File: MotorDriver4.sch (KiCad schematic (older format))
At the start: 38 parts, among them J24 43045-0802, J25 53426-0410, U49 MAX40056FAUA+, U50 DRV8312DDWR, U51 MAX40056FAUA+, U52 MIC2090-2YM5-TR

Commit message: PVT
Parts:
- C200: renamed from C208; footprint Capacitor-Chip:C_CHIP_1608_Reflow -> Capacitor-Chip:C_CHIP_1005_Hand_NoSilk; PartName GRM188R61E105KA12D -> TMK105BJ105MV-F
- C201: renamed from C209; PartName C1005X5R1V105K050BE -> TMK105BJ105MV-F
- C202: renamed from C210; PartName C1005X5R1V105K050BE -> TMK105BJ105MV-F
- C203: renamed from C211; footprint Capacitor-Chip:C_CHIP_1608_Reflow -> Capacitor-Chip:C_CHIP_1005_Hand_NoSilk; PartName GRM188R61E105KA12D -> TMK105BJ105MV-F
- C204: renamed from C212; footprint Capacitor-Chip:C_CHIP_1608_Reflow -> Capacitor-Chip:C_CHIP_1005_Hand_NoSilk; PartName GRM188R61E105KA12D -> TMK105BJ105MV-F
- C205: renamed from C213; footprint Capacitor-Chip:C_CHIP_1608_Reflow -> Capacitor-Chip:C_CHIP_1005_Hand_NoSilk; PartName GRM188R61E105KA12D -> TMK105BJ105MV-F
- C207: renamed from C215; PartName C1005X5R1V105K050BE -> TMK105BJ105MV-F
- C208: renamed from C216; PartName C1005X5R1V105K050BE -> TMK105BJ105MV-F
- C216: renamed from C224; PartName C1005X5R1V105K050BE -> TMK105BJ105MV-F
- R110: renamed from R125; value 2m -> 3m; PartName PMR18EZPJV2L0 -> PMR18EZPFV3L00
- R111: renamed from R126; value 2m -> 3m; PartName PMR18EZPJV2L0 -> PMR18EZPFV3L00
- renumbered C214 to C206, C217 to C209, C218 to C210, C219 to C211, C220 to C212, C221 to C213, C222 to C214, C223 to C215, L22 to L18, L23 to L19, L24 to L20, R121 to R106, R122 to R107, R123 to R108, R124 to R109, R127 to R112, R128 to R113, RA27 to RA28, RA28 to RA29, RA29 to RA30, U49 to U46, U50 to U47, U51 to U48, U52 to U49

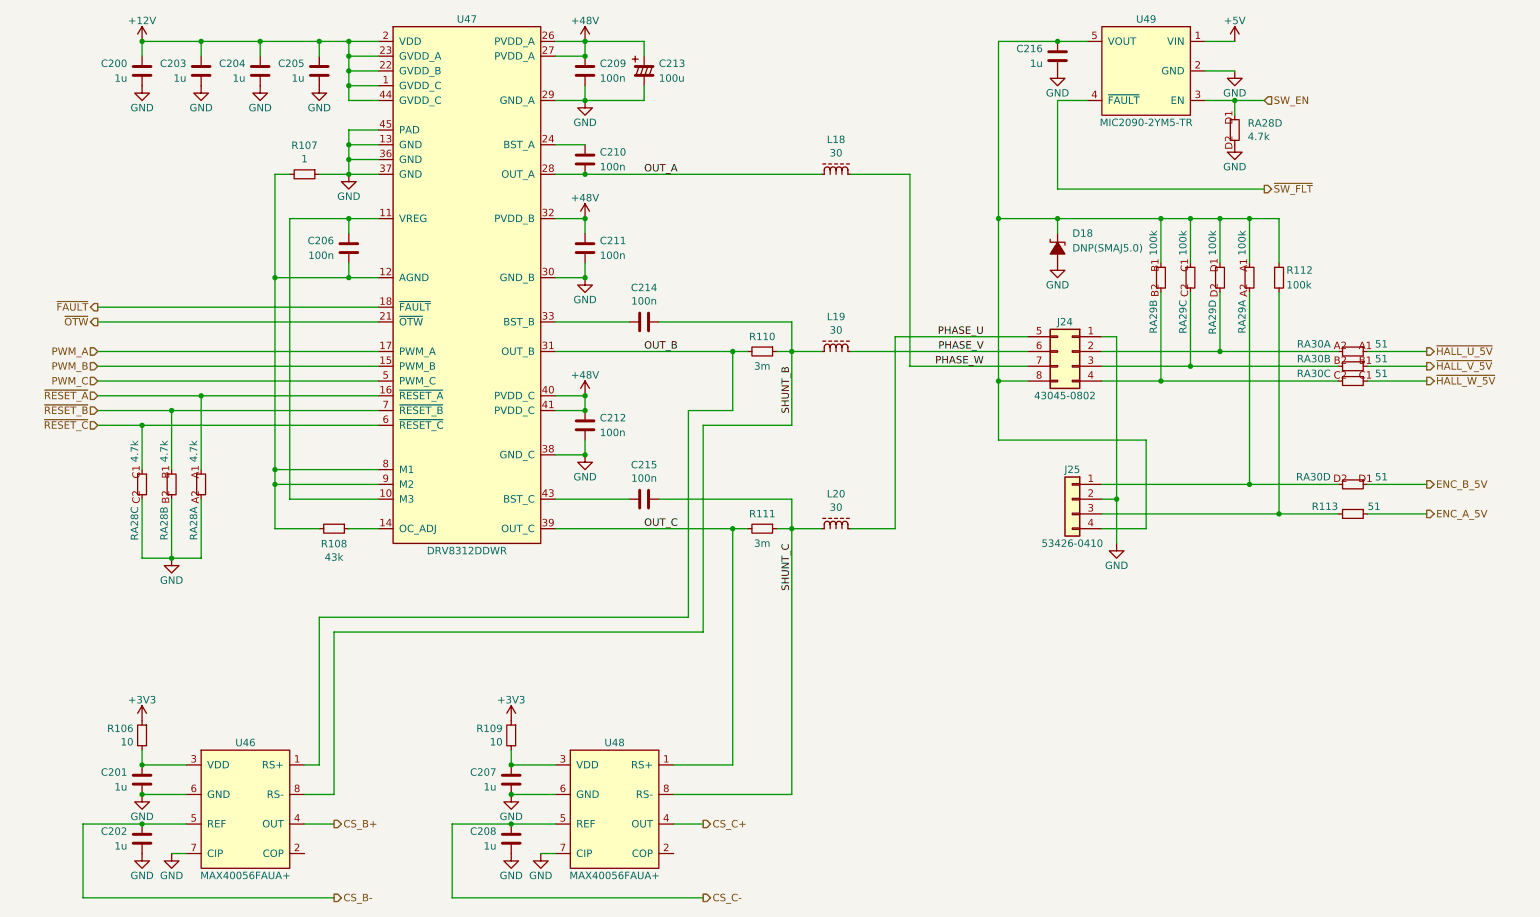
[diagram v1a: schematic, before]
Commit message: SBUにTVSダイオードを追加
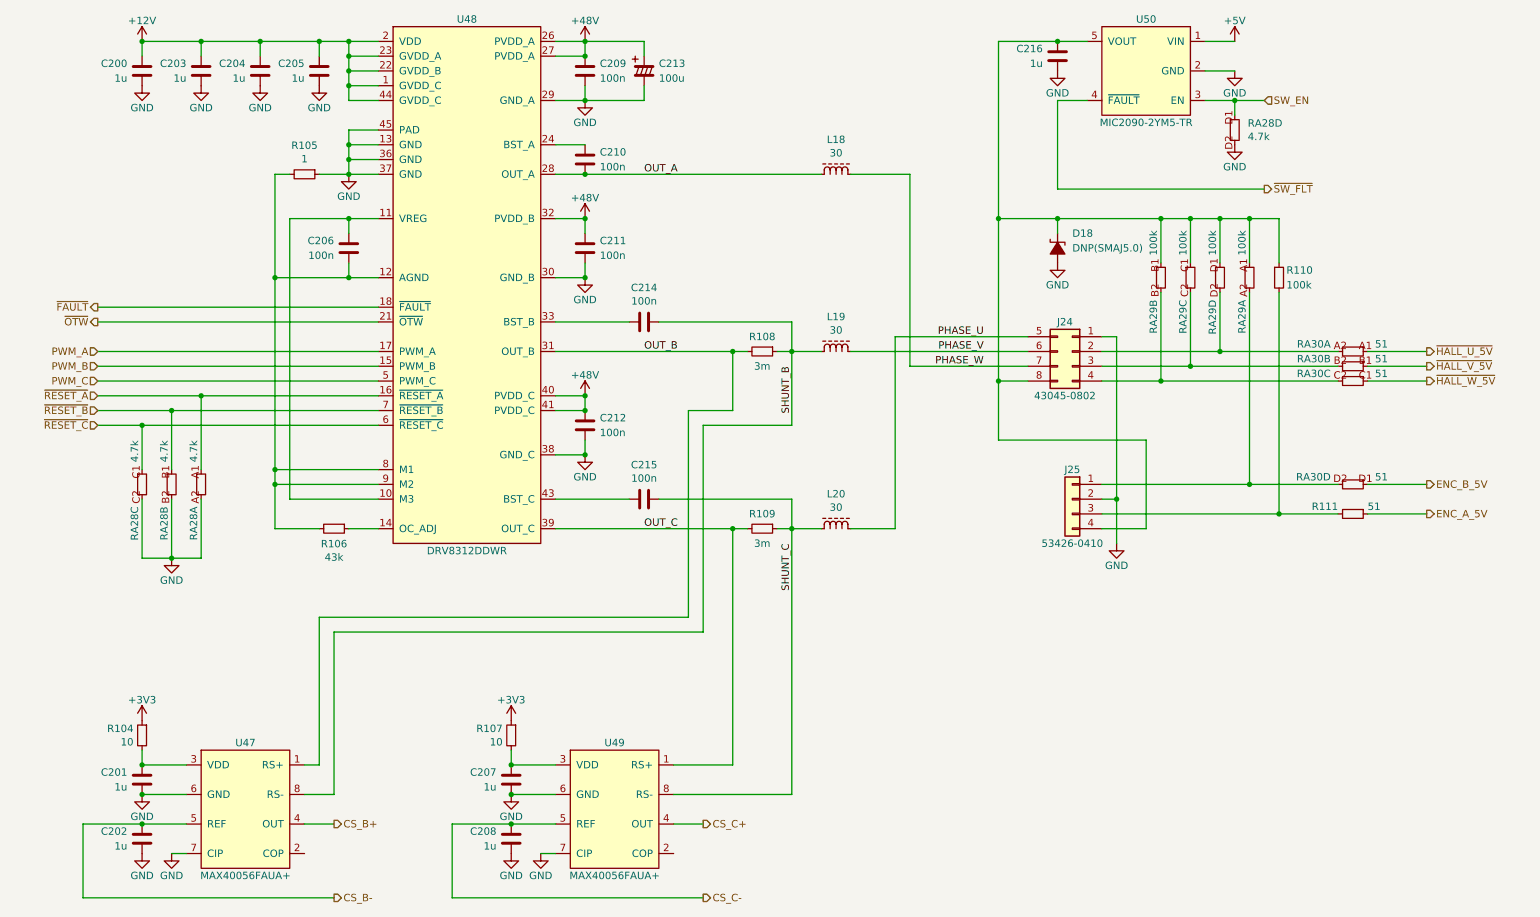
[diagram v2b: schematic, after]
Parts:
- renumbered R106 to R104, R107 to R105, R108 to R106, R109 to R107, R110 to R108, R111 to R109, R112 to R110, R113 to R111, U46 to U47, U47 to U48, U48 to U49, U49 to U50
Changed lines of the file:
@@
 AR Path="/5F237486/5E61F4E9" Ref="U?"  Part="1"
 AR Path="/5F259EEE/5E61F4E9" Ref="U?"  Part="1"
-AR Path="/5F259F7D/5E61F4E9" Ref="U47"  Part="1"
-F 0 "U47" H 4000 4750 50  0000 C CNN
+AR Path="/5F259F7D/5E61F4E9" Ref="U48"  Part="1"
+F 0 "U48" H 4000 4750 50  0000 C CNN
 F 1 "DRV8312DDWR" H 4000 1150 50  0000 C CNN
 F 2 "IC-SOP:HTSSOP44-W6.1_EP4.31x8.26" H 4000 2900 50  0001 C CNN
@@
 AR Path="/5F237486/5E61F5D9" Ref="R?"  Part="1"
 AR Path="/5F259EEE/5E61F5D9" Ref="R?"  Part="1"
-AR Path="/5F259F7D/5E61F5D9" Ref="R107"  Part="1"
-F 0 "R107" V 2705 2100 50  0000 C CNN
+AR Path="/5F259F7D/5E61F5D9" Ref="R105"  Part="1"
+F 0 "R105" V 2705 2100 50  0000 C CNN
 F 1 "1" V 2796 2100 50  0000 C CNN
 F 2 "Resistor-Chip:R_CHIP_1005_Hand_NoSilk" V 2950 2000 50  0001 C CNN
@@
 AR Path="/5F237486/5E61F5E3" Ref="R?"  Part="1"
 AR Path="/5F259EEE/5E61F5E3" Ref="R?"  Part="1"
-AR Path="/5F259F7D/5E61F5E3" Ref="R108"  Part="1"
-F 0 "R108" V 3203 4500 50  0000 C CNN
+AR Path="/5F259F7D/5E61F5E3" Ref="R106"  Part="1"
+F 0 "R106" V 3203 4500 50  0000 C CNN
 F 1 "43k" V 3294 4500 50  0000 C CNN
 F 2 "Resistor-Chip:R_CHIP_1005_Hand_NoSilk" V 3150 4400 50  0001 C CNN
@@
 AR Path="/5F237486/5E61F5F8" Ref="R?"  Part="1"
 AR Path="/5F259EEE/5E61F5F8" Ref="R?"  Part="1"
-AR Path="/5F259F7D/5E61F5F8" Ref="R111"  Part="1"
-F 0 "R111" V 5900 4500 50  0000 C CNN
+AR Path="/5F259F7D/5E61F5F8" Ref="R109"  Part="1"
+F 0 "R109" V 5900 4500 50  0000 C CNN
 F 1 "3m" V 6100 4500 50  0000 C CNN
 F 2 "Resistor-Chip:R_CHIP_3216_Reflow" V 6050 4400 50  0001 C CNN
@@
 AR Path="/5F237486/5E61F605" Ref="R?"  Part="1"
 AR Path="/5F259EEE/5E61F605" Ref="R?"  Part="1"
-AR Path="/5F259F7D/5E61F605" Ref="R110"  Part="1"
-F 0 "R110" V 5900 3300 50  0000 C CNN
+AR Path="/5F259F7D/5E61F605" Ref="R108"  Part="1"
+F 0 "R108" V 5900 3300 50  0000 C CNN
 F 1 "3m" V 6100 3300 50  0000 C CNN
 F 2 "Resistor-Chip:R_CHIP_3216_Reflow" V 6050 3200 50  0001 C CNN
@@
 AR Path="/5F259EEE/5F1F5EA4" Ref="U?"  Part="1"
 AR Path="/5F259F40/5F1F5EA4" Ref="U?"  Part="1"
-AR Path="/5F259F7D/5F1F5EA4" Ref="U49"  Part="1"
-F 0 "U49" H 8600 1750 50  0000 C CNN
+AR Path="/5F259F7D/5F1F5EA4" Ref="U50"  Part="1"
+F 0 "U50" H 8600 1750 50  0000 C CNN
 F 1 "MIC2090-2YM5-TR" H 8600 1050 50  0000 C CNN
 F 2 "IC-SOT:SOT23-5" H 8600 1400 50  0001 C CNN
@@
 AR Path="/5F235A43/5F4ED90C" Ref="U?"  Part="1"
 AR Path="/5F237486/5F4ED90C" Ref="U?"  Part="1"
-AR Path="/5F259F7D/5F4ED90C" Ref="U46"  Part="1"
-F 0 "U46" H 2500 6850 50  0000 C CNN
+AR Path="/5F259F7D/5F4ED90C" Ref="U47"  Part="1"
+F 0 "U47" H 2500 6850 50  0000 C CNN
 F 1 "MAX40056FAUA+" H 2500 5950 50  0000 C CNN
 F 2 "IC-SOP:MSOP8" H 2500 6400 50  0001 C CNN
@@
 AR Path="/5F235A43/5F4ED912" Ref="U?"  Part="1"
 AR Path="/5F237486/5F4ED912" Ref="U?"  Part="1"
-AR Path="/5F259F7D/5F4ED912" Ref="U48"  Part="1"
-F 0 "U48" H 5000 6850 50  0000 C CNN
+AR Path="/5F259F7D/5F4ED912" Ref="U49"  Part="1"
+F 0 "U49" H 5000 6850 50  0000 C CNN
 F 1 "MAX40056FAUA+" H 5000 5950 50  0000 C CNN
 F 2 "IC-SOP:MSOP8" H 5000 6400 50  0001 C CNN
@@
 AR Path="/5F235A43/5F4ED978" Ref="R?"  Part="1"
 AR Path="/5F237486/5F4ED978" Ref="R?"  Part="1"
-AR Path="/5F259F7D/5F4ED978" Ref="R106"  Part="1"
-F 0 "R106" H 1858 5946 50  0000 L CNN
+AR Path="/5F259F7D/5F4ED978" Ref="R104"  Part="1"
+F 0 "R104" H 1858 5946 50  0000 L CNN
 F 1 "10" H 1858 5855 50  0000 L CNN
 F 2 "Resistor-Chip:R_CHIP_1005_Hand_NoSilk" V 1850 5800 50  0001 C CNN
@@
 AR Path="/5F235A43/5F4ED97E" Ref="R?"  Part="1"
 AR Path="/5F237486/5F4ED97E" Ref="R?"  Part="1"
-AR Path="/5F259F7D/5F4ED97E" Ref="R109"  Part="1"
-F 0 "R109" H 4358 5946 50  0000 L CNN
+AR Path="/5F259F7D/5F4ED97E" Ref="R107"  Part="1"
+F 0 "R107" H 4358 5946 50  0000 L CNN
 F 1 "10" H 4358 5855 50  0000 L CNN
 F 2 "Resistor-Chip:R_CHIP_1005_Hand_NoSilk" V 4350 5800 50  0001 C CNN
@@
 P 10000 4400
 AR Path="/5F235A43/5EA40EFB" Ref="R?"  Part="1"
-AR Path="/5F259F7D/5EA40EFB" Ref="R113"  Part="1"
-F 0 "R113" V 9950 4300 50  0000 R CNN
+AR Path="/5F259F7D/5EA40EFB" Ref="R111"  Part="1"
+F 0 "R111" V 9950 4300 50  0000 R CNN
 F 1 "51" V 9950 4500 50  0000 L CNN
 F 2 "Resistor-Chip:R_CHIP_1005_Hand_NoSilk" V 10050 4300 50  0001 C CNN
@@
 P 9500 2800
 AR Path="/5F235A43/5EA9B0A9" Ref="R?"  Part="1"
-AR Path="/5F259F7D/5EA9B0A9" Ref="R112"  Part="1"
-F 0 "R112" H 9550 2850 50  0000 L CNN
+AR Path="/5F259F7D/5EA9B0A9" Ref="R110"  Part="1"
+F 0 "R110" H 9550 2850 50  0000 L CNN
 F 1 "100k" H 9550 2750 50  0000 L CNN
 F 2 "Resistor-Chip:R_CHIP_1005_Hand_NoSilk" V 9550 2700 50  0001 C CNN
